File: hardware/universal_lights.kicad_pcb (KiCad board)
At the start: 2 copper layers, 100 x 15 mm, 27 parts, among them J1 entrada, J2 salida, J3 DIP-BLACK-MALE-HEADER_2X3P-2.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, J4 Conn_01x08, J5 Conn_01x02, Q1 NPN, U1 ATTINY88-AU

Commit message: WIP del atmega 328 para ADCtouch
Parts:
- added G***: LOGO, LOGO, B.Cu at (140.0, 142.0)

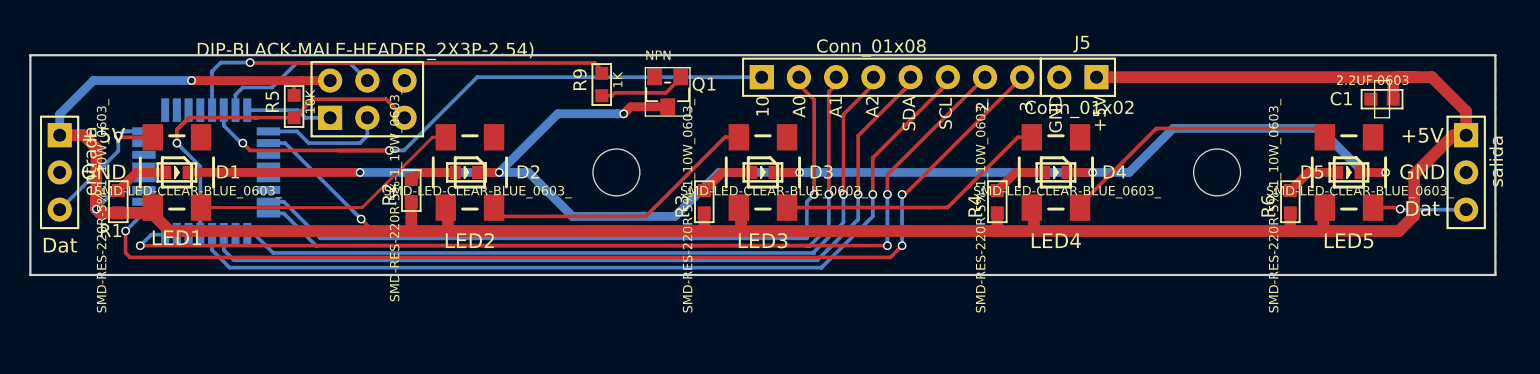
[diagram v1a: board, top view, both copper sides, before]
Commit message: instalado atmega 328, ajustados agujeros de montaje, cambio silk versión
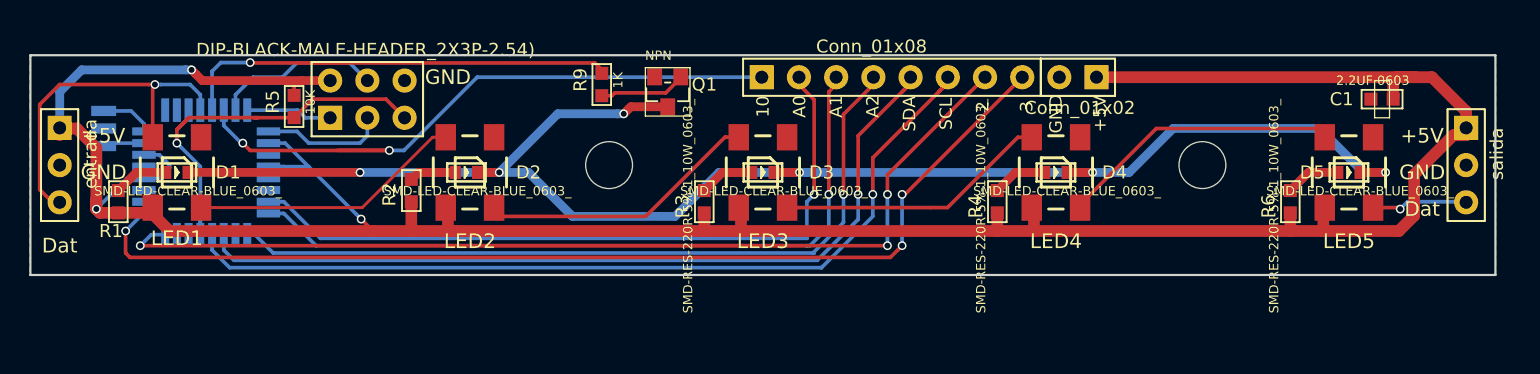
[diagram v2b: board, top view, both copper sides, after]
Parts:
- removed the G*** at (140.0, 142.0)
- removed the REF** at (90.0, 143.0)
- removed the REF** at (131.0, 143.0)
- added G***: LOGO, kicad_libs:logo_chip_negativo, B.Cu at (139.5, 141.5)
- added REF**: MountingHole_3.2mm_M3_DIN965, Mounting_Holes:MountingHole_3.2mm_M3_DIN965, F.Cu at (130.0, 142.5)
- added REF**: MountingHole_3.2mm_M3_DIN965, Mounting_Holes:MountingHole_3.2mm_M3_DIN965, F.Cu at (89.5, 142.5)
- added Y1: 16Mhz, SeeedOPL-Crystal Oscillator-2016:X3-SMD-3.6X1.3X0.8MM, B.Cu at (55.0, 140.0)
- U1: value ATTINY88-AU -> ATmega328P-AU
- moved J1 0.50 mm to (52.0, 142.5)
- moved J2 0.50 mm to (148.0, 142.5)
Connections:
- U1 pad 12: (no net) -> /datos_led_in
- U1 pad 20: (no net) -> +5V
- U1 pad 3: (no net) -> GND
- U1 pad 6: (no net) -> +5V
- U1 pad 7: (no net) -> Net-(U1-Pad7)
- U1 pad 8: /datos_led_in -> Net-(U1-Pad8)
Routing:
- net /datos_led_in: track 11.6 -> 24.3 mm
- net +5V: track 187.5 -> 196.6 mm
- net Net-(U1-Pad8): track 0.00 -> 3.64 mm
- net Net-(U1-Pad7): track 0.00 -> 2.83 mm
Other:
- board text added: "2018 ASC"
- board text added: "Fum Blau SCV Universal Lamp v3"
- board text removed: "2017 ASC"
- board text removed: "Fum Blau SCV Universal Lamp v2"

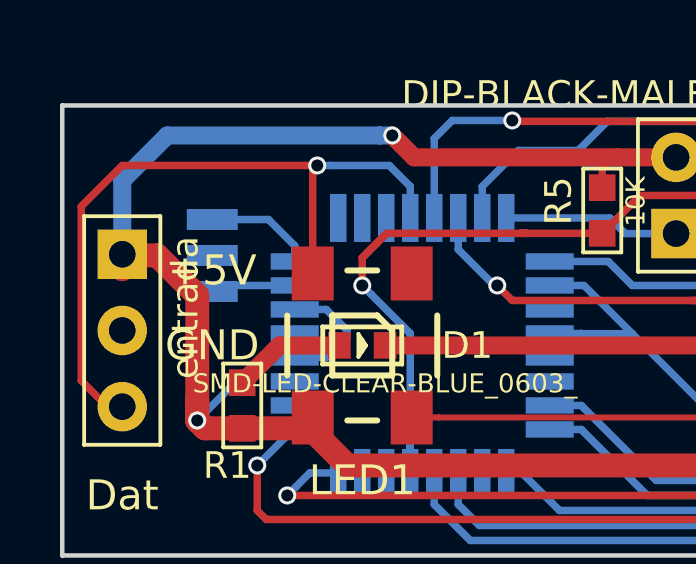
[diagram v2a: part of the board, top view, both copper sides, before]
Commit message: añado 470R a entrada datos led, muevo cristal para que sea mas facil de soldar
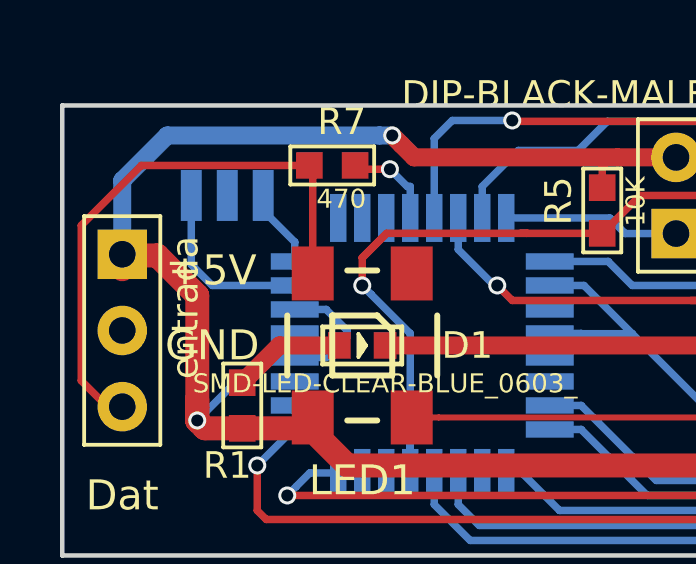
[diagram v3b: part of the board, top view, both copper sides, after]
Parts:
- added R7: 470, SeeedOPL-Resistor-2016:R0603, F.Cu at (59.0, 137.0)
- moved Y1 2.06 mm to (55.5, 138.0), turned to 180 degrees
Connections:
- U1 pad 12: /datos_led_in -> Net-(R7-Pad1)
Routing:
- net /datos_led_in: track 24.3 -> 19.2 mm, vias 1 -> 0
- net Net-(U1-Pad7): track 2.83 -> 6.04 mm
- net Net-(R7-Pad1): track 0.00 -> 3.18 mm, vias 0 -> 1
- net Net-(U1-Pad8): track 3.64 -> 2.64 mm
